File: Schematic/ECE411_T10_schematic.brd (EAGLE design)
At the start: 100 x 80 mm, 61 parts, among them IC1 LM386MM-1, J1 1, J2 DCJ0202, J3 AVR_SPI_PRG_6PTH, Q1 8.192 MHz, U1 ATMEGA328P_PDIP

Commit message: layout preliminary final
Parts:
- removed SM1: 06FLZ-SM1, con-jst:6FLZ-SM
- removed TP31, TP32: TPB1,27, testpad:B1,27
- added C11: 100nF, adafruit:C025-024X044
- added JP1: (no value), pinhead:1X08
- added TP33, TP34, TP35, TP36: TPB1,27, testpad:B1,27
- moved TP11 69.9 mm to (63.5, 48.3)
- moved TP22 67.6 mm to (68.6, 30.5)
- moved TP10 67.3 mm to (64.8, 45.7)
- moved TP26 63.7 mm to (61.0, 12.7)
- moved TP16 63.5 mm to (64.8, 52.1)
- moved TP18 62.9 mm to (64.8, 20.3)
- moved TP9 61.3 mm to (62.2, 43.2)
- moved TP27 60.8 mm to (62.2, 16.5)
- moved TP30 59.3 mm to (43.2, 44.5)
- moved TP12 58.5 mm to (61.0, 27.9)
- moved TP25 57.9 mm to (61.0, 22.9)
- moved TP15 57.5 mm to (59.7, 50.8)
- moved TP23 51.7 mm to (26.7, 58.4)
- moved TP21 50.0 mm to (31.8, 57.1)
- moved TP20 45.5 mm to (29.2, 57.1)
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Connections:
- new net N$33: JP1.2, TP36.TP
- new net N$34: JP1.3, TP35.TP
- new net N$35: JP1.4, TP34.TP
- new net N$36: JP1.5, TP33.TP
- net GND: now also C11.2, JP1.8; no longer SM1.6
- net SM1-CLK: now also JP1.6; no longer SM1.3
- net SM1-DAT: now also JP1.7; no longer SM1.5
- net VIN: now also C11.1, JP1.1; no longer SM1.1, TP31.TP, TP32.TP
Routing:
- net RST: track 208.2 -> 69.4 mm, vias 0 -> 1
- net 3.3V: track 134.5 -> 8.17 mm, vias 1 -> 0
- net N$18: track 153.3 -> 30.0 mm, vias 2 -> 0
- net VIN: track 270.9 -> 159.5 mm, vias 4 -> 2
- net N$20: track 125.5 -> 19.8 mm, vias 1 -> 0
- net N$29: track 104.2 -> 9.42 mm, vias 0 -> 1
- net N$19: track 108.9 -> 19.1 mm, vias 2 -> 0
- net N$30: track 84.9 -> 8.17 mm, vias 1 -> 0
- net GND: track 312.9 -> 240.0 mm, vias 3 -> 0
- net N$31: track 92.7 -> 20.6 mm, vias 1 -> 0
- net N$11: track 91.3 -> 19.5 mm, vias 1 -> 0
- net SCL_5.0V: track 111.9 -> 43.1 mm, vias 2 -> 0
- net N$12: track 94.3 -> 26.2 mm, vias 1 -> 0
- net SDA_5.0V: track 106.6 -> 39.3 mm, vias 2 -> 0
- net N$28: track 59.6 -> 6.88 mm, vias 3 -> 0
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- added copper zone on layer 16, net GND
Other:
- board size 100 x 80 mm -> 68.7 x 59.7 mm
- board text added: "T10: Color Sensing Infinity Mirror J. Scott, C. Ciobanu, D. Denhart, N. Lynch-Jonely ECE 411 - Practicum Project v1.0: 11/5/2014"

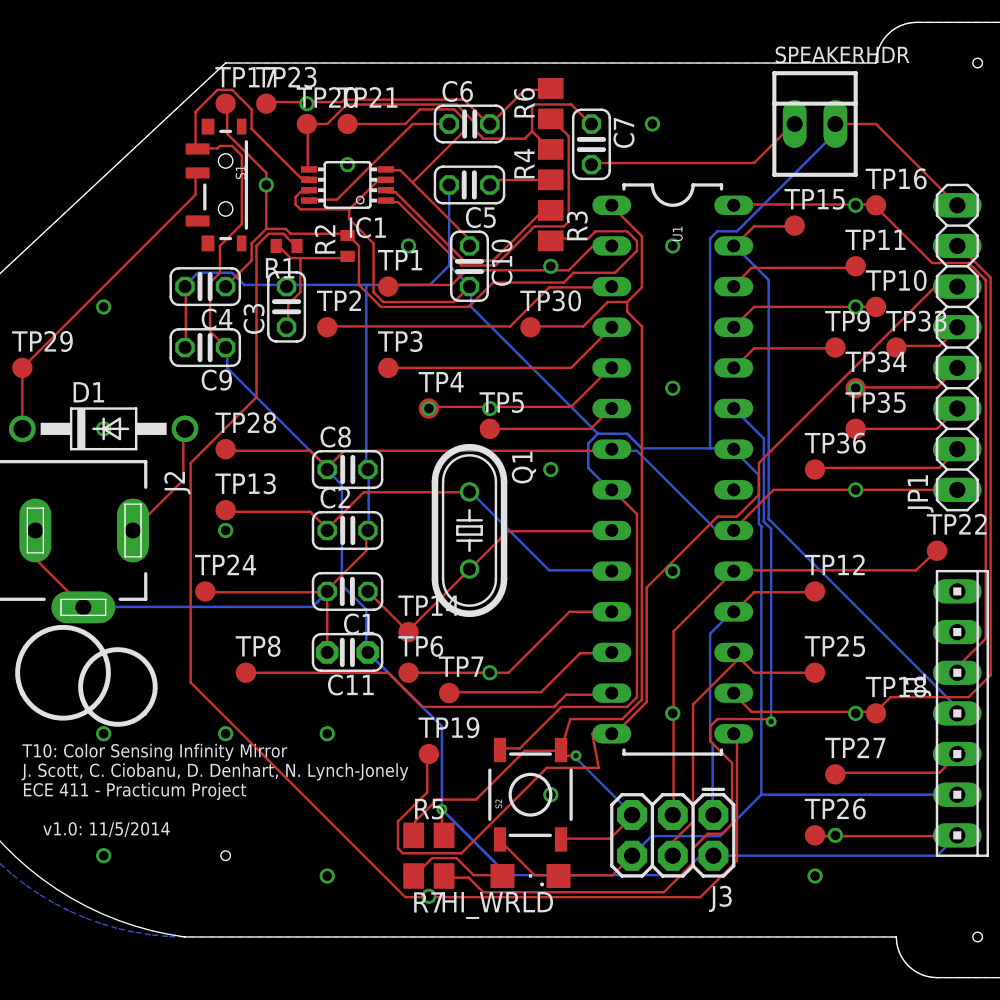
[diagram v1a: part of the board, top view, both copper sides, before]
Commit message: reran DRC
errors from vias.. what even happened to my ground plane. ugh.
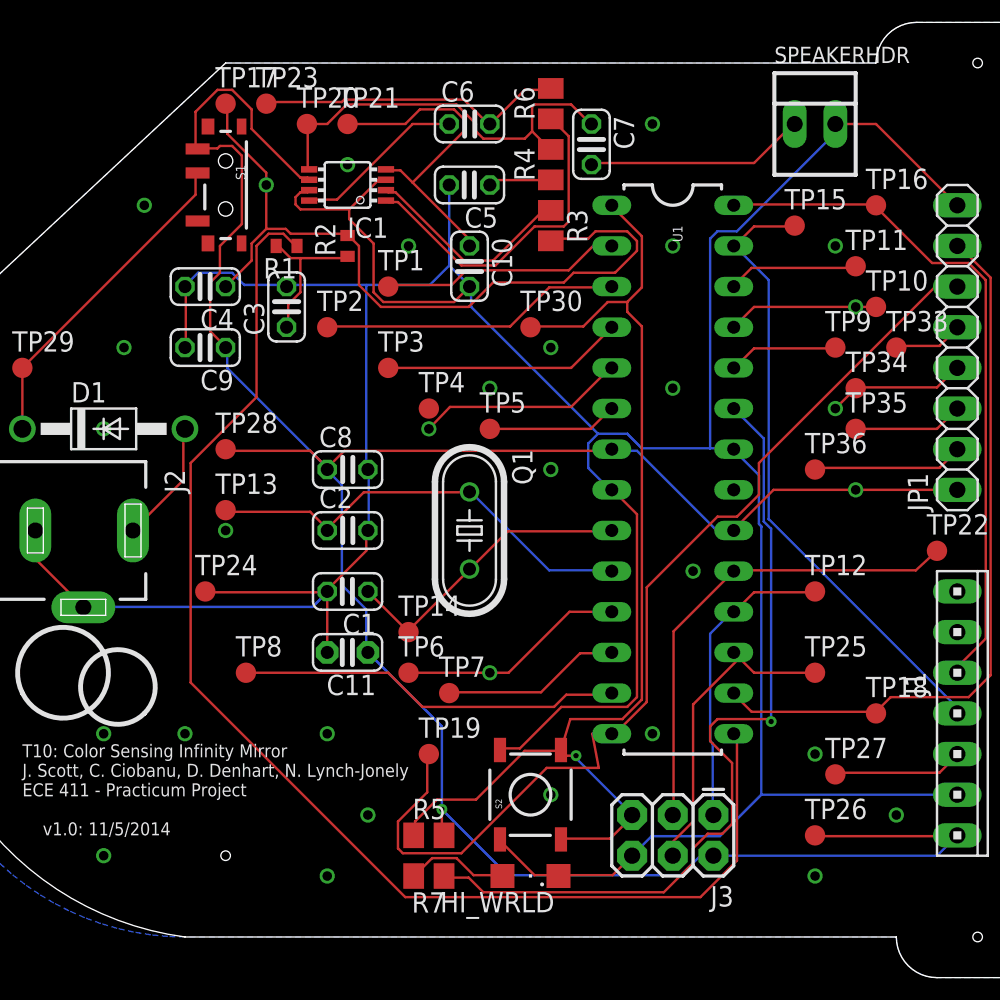
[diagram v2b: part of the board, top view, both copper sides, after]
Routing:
- net N$35: track 6.88 -> 8.67 mm
- net N$24: track 12.5 -> 13.0 mm
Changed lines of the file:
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@@
 <contactref element="U1" pad="5"/>
 <contactref element="TP4" pad="TP"/>
-<wire x1="45.72" y1="39.4716" x2="36.8808" y2="39.4716" width="0.1524" layer="1"/>
+<wire x1="45.72" y1="39.4716" x2="38.1508" y2="39.4716" width="0.1524" layer="1"/>
 <wire x1="48.1584" y1="41.91" x2="45.72" y2="39.4716" width="0.1524" layer="1"/>
-<wire x1="36.8808" y1="39.4716" x2="36.83" y2="39.37" width="0.1524" layer="1"/>
+<wire x1="38.1508" y1="39.4716" x2="36.83" y2="38.1" width="0.1524" layer="1"/>
 <wire x1="48.1584" y1="41.91" x2="48.26" y2="41.91" width="0.1524" layer="1"/>
-<via x="36.83" y="39.37" extent="1-16" drill="0.6" shape="square"/>
+<via x="36.83" y="38.1" extent="1-16" drill="0.6" shape="square"/>
 </signal>
 <signal name="N$25">
@@
 <wire x1="68.58" y1="40.6908" x2="63.5508" y2="40.6908" width="0.1524" layer="1"/>
 <wire x1="69.7992" y1="41.91" x2="68.58" y2="40.6908" width="0.1524" layer="1"/>
-<wire x1="63.5508" y1="40.6908" x2="63.5" y2="40.64" width="0.1524" layer="1"/>
+<wire x1="63.5508" y1="40.6908" x2="62.23" y2="39.37" width="0.1524" layer="1"/>
 <wire x1="69.7992" y1="41.91" x2="69.85" y2="41.91" width="0.1524" layer="1"/>
-<via x="63.5" y="40.64" extent="1-16" drill="0.6" shape="square"/>
+<via x="62.23" y="39.37" extent="1-16" drill="0.6" shape="square"/>
 </signal>
 <signal name="N$36">
@@
 </signal>
 <signal name="N$38">
-<via x="52.07" y="20.32" extent="1-16" drill="0.6" shape="square"/>
+<via x="50.8" y="19.05" extent="1-16" drill="0.6" shape="square"/>
 </signal>
 <signal name="N$39">
-<via x="52.07" y="29.21" extent="1-16" drill="0.6" shape="square"/>
+<via x="53.34" y="29.21" extent="1-16" drill="0.6" shape="square"/>
 </signal>
 <signal name="N$40">
@@
 </signal>
 <signal name="N$45">
-<via x="24.13" y="19.05" extent="1-16" drill="0.6" shape="square"/>
+<via x="21.59" y="19.05" extent="1-16" drill="0.6" shape="square"/>
 </signal>
 <signal name="N$46">
@@
 </signal>
 <signal name="N$49">
-<via x="63.5" y="52.07" extent="1-16" drill="0.6" shape="square"/>
+<via x="62.23" y="49.53" extent="1-16" drill="0.6" shape="square"/>
 </signal>
 <signal name="N$50">
@@
 </signal>
 <signal name="N$51">
-<via x="63.5" y="20.32" extent="1-16" drill="0.6" shape="square"/>
+<via x="60.96" y="17.78" extent="1-16" drill="0.6" shape="square"/>
 </signal>
 <signal name="N$52">
-<via x="62.23" y="12.7" extent="1-16" drill="0.6" shape="square"/>
+<via x="66.04" y="13.97" extent="1-16" drill="0.6" shape="square"/>
 </signal>
 <signal name="N$53">
@@
 </signal>
 <signal name="N$55">
-<via x="40.64" y="39.37" extent="1-16" drill="0.6" shape="square"/>
+<via x="40.64" y="40.64" extent="1-16" drill="0.6" shape="square"/>
 </signal>
 <signal name="N$56">
@@
 </signal>
 <signal name="N$57">
-<via x="29.21" y="58.42" extent="1-16" drill="0.6" shape="square"/>
+<via x="19.05" y="52.07" extent="1-16" drill="0.6" shape="square"/>
 </signal>
 <signal name="N$58">
-<via x="44.45" y="48.26" extent="1-16" drill="0.6" shape="square"/>
+<via x="44.45" y="43.18" extent="1-16" drill="0.6" shape="square"/>
 </signal>
 <signal name="N$59">
-<via x="16.51" y="45.72" extent="1-16" drill="0.6" shape="square"/>
+<via x="17.78" y="43.18" extent="1-16" drill="0.6" shape="square"/>
 </signal>
 <signal name="N$60">
-<via x="36.83" y="8.89" extent="1-16" drill="0.6" shape="square"/>
+<via x="33.02" y="13.97" extent="1-16" drill="0.6" shape="square"/>
 </signal>
 </signals>

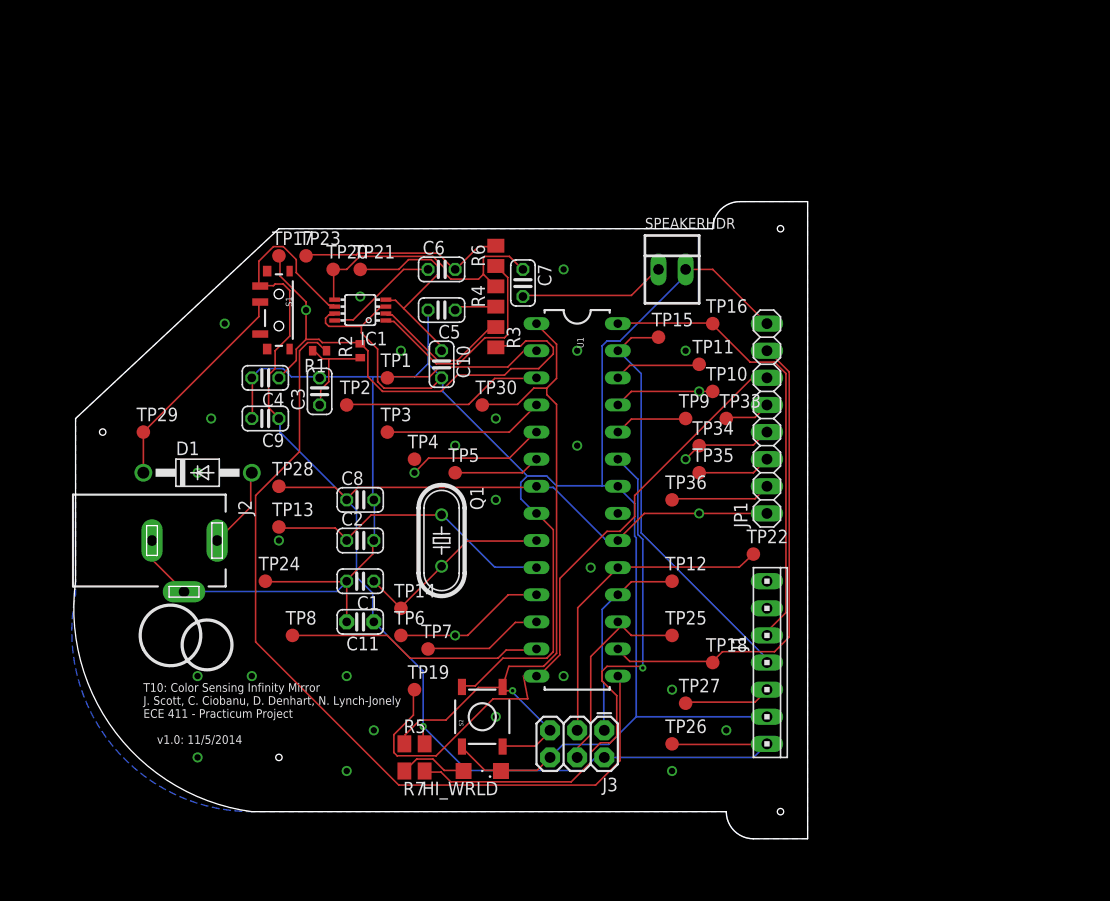
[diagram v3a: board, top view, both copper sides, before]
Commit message: Preliminary board 2: electric boogaloo
completely rerouted the board with the correct size traces!
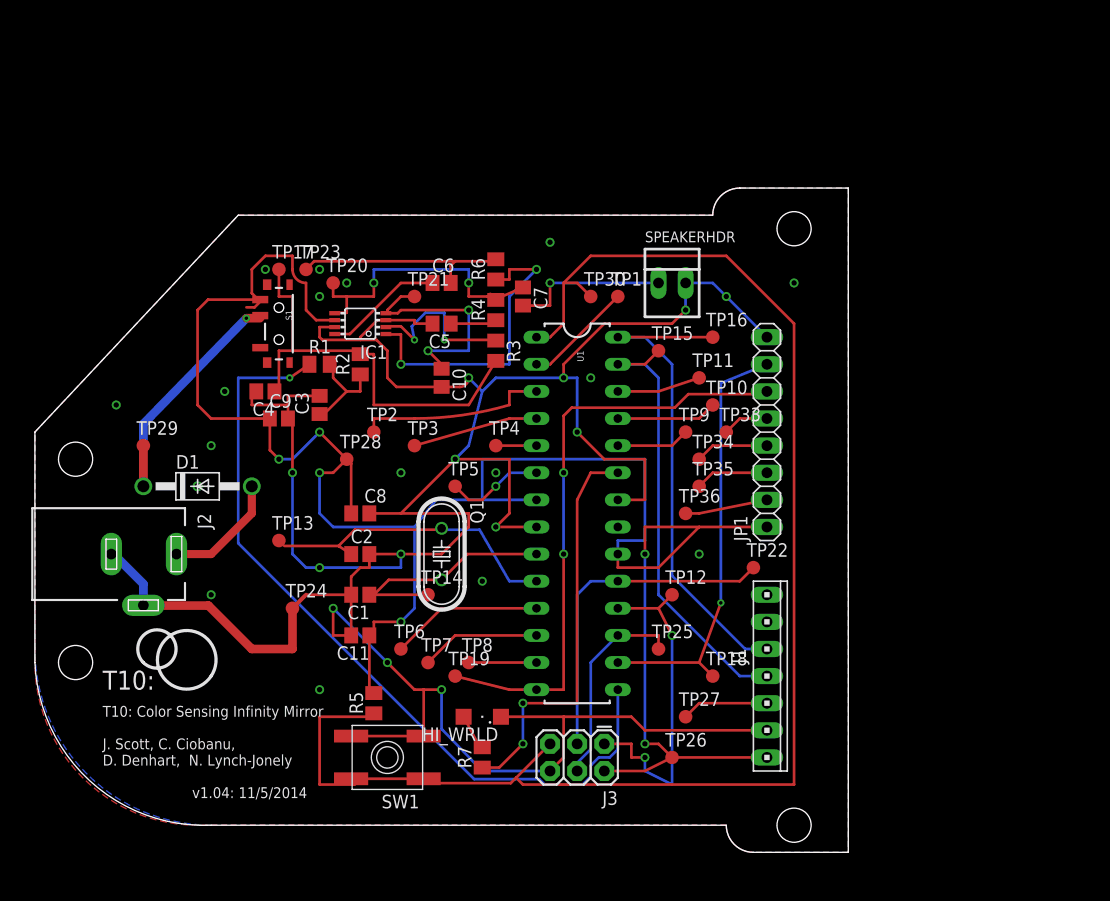
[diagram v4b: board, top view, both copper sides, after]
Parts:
- removed S2: TAC_SWITCHSMD, SparkFun-Electromechanical:TACTILE-SWITCH-SMD
- added SW1: SPST_TACT-EVQQ2, adafruit:EVQ-Q2
- C1, C10, C2, C3, C4, C5, C6, C7, C8, C9: device resistor:C025-024X044 -> adafruit:C0805
- C11: device adafruit:C025-024X044 -> adafruit:C0805
- R1, R2: device resistor:R0402 -> adafruit:M0805
- moved TP1 22.9 mm to (55.9, 54.6)
- moved TP8 16.7 mm to (41.9, 20.3)
- moved TP30 14.4 mm to (53.3, 54.6)
- moved TP4 7.73 mm to (44.5, 40.6)
- moved TP28 6.84 mm to (30.5, 39.4)
- moved R7 6.48 mm to (43.2, 11.4), turned to 90 degrees
- moved TP21 5.68 mm to (36.8, 54.6)
- moved R5 5.39 mm to (33.0, 16.5), turned to 90 degrees
- moved HI_WRLD 5.08 mm to (43.2, 15.2)
- moved TP19 4.02 mm to (40.6, 19.1)
- moved J2 4.02 mm to (11.4, 30.5)
- moved TP2 3.59 mm to (33.0, 41.9)
- moved TP24 3.59 mm to (25.4, 25.4)
- moved TP14 2.84 mm to (38.1, 26.7)
- moved TP3 2.84 mm to (36.8, 40.6)
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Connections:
- net GND: now also SW1.A, SW1.A'; no longer S2.1, S2.2
- net RST: now also SW1.B, SW1.B'; no longer S2.3, S2.4
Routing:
- net RST: track 69.4 -> 141.0 mm, vias 1 -> 0
- net GND: track 240.0 -> 287.3 mm, vias 0 -> 13
- net VIN: track 159.5 -> 197.8 mm, vias 2 -> 6
- net N$27: track 24.1 -> 6.35 mm
- net N$10: track 52.0 -> 38.0 mm, vias 1 -> 2
- net N$19: track 19.1 -> 31.6 mm, vias 0 -> 2
- net N$24: track 13.0 -> 3.81 mm, vias 1 -> 0
- net N$3: track 21.1 -> 29.1 mm, vias 0 -> 2
- net SM1-CLK: track 63.5 -> 56.0 mm, vias 0 -> 2
- net N$6: track 48.2 -> 40.7 mm, vias 1 -> 0
- net N$4: track 80.8 -> 75.0 mm, vias 0 -> 1
- net N$16: track 15.1 -> 10.3 mm
- net SM1-DAT: track 45.4 -> 40.6 mm, vias 0 -> 1
- net N$15: track 20.5 -> 25.0 mm, vias 0 -> 1
- net N$13: track 7.76 -> 11.2 mm
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- added copper zone on layer 1, net GND
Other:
- board size 68.7 x 59.7 mm -> 76.2 x 62.2 mm
- board text added: "T10:"
- board text added: "T10: Color Sensing Infinity Mirror J. Scott, C. Ciobanu, D. Denhart, N. Lynch-Jonely v1.04: 11/5/2014"
- board text removed: "T10: Color Sensing Infinity Mirror J. Scott, C. Ciobanu, D. Denhart, N. Lynch-Jonely ECE 411 - Practicum Project v1.0: 11/5/2014"
